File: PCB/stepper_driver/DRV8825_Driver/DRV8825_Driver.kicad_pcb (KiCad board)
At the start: 2 copper layers, 39.6 x 35.8 mm, 21 parts, among them J1 Conn_01x04_Pin, J2 Conn_01x02_Pin, J3 Conn_01x02_Pin, SW1 SW_DIP_x03, U1 DRV8825PWP

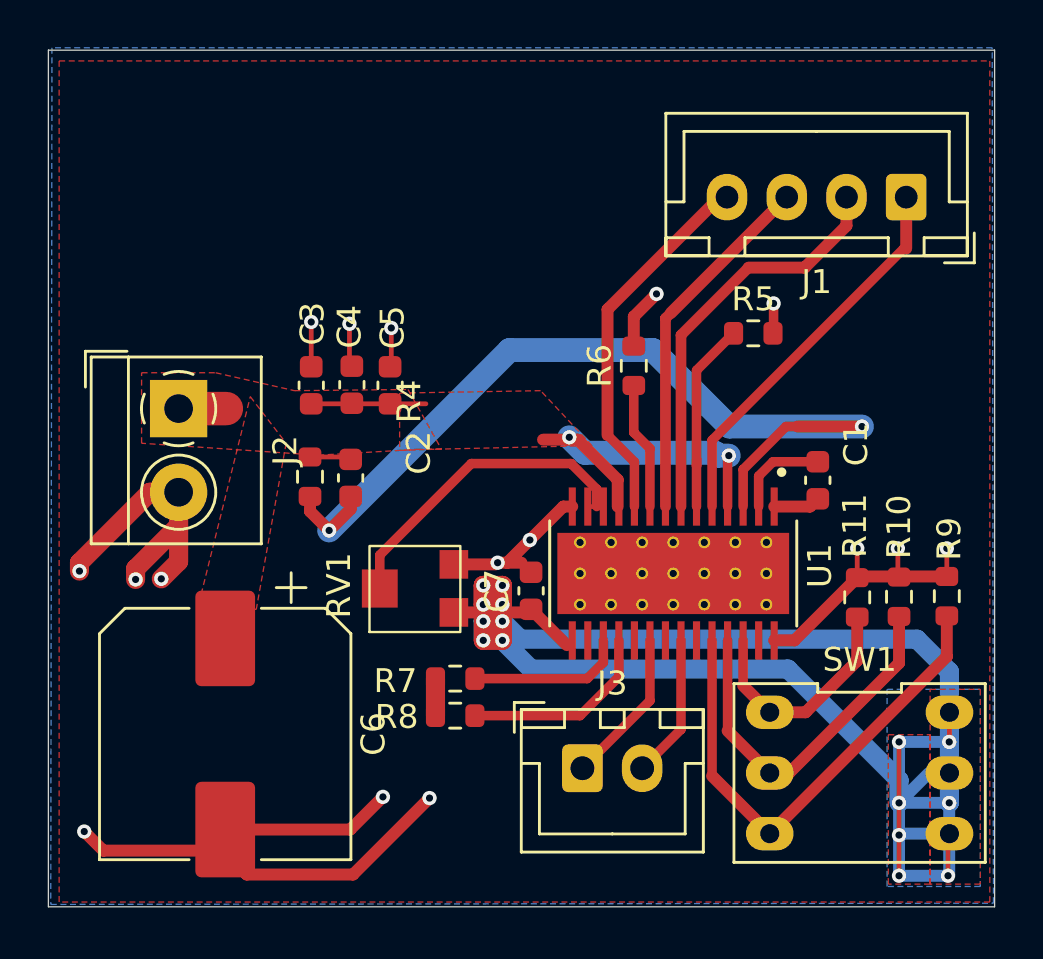
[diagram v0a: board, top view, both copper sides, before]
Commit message: footprint reduction
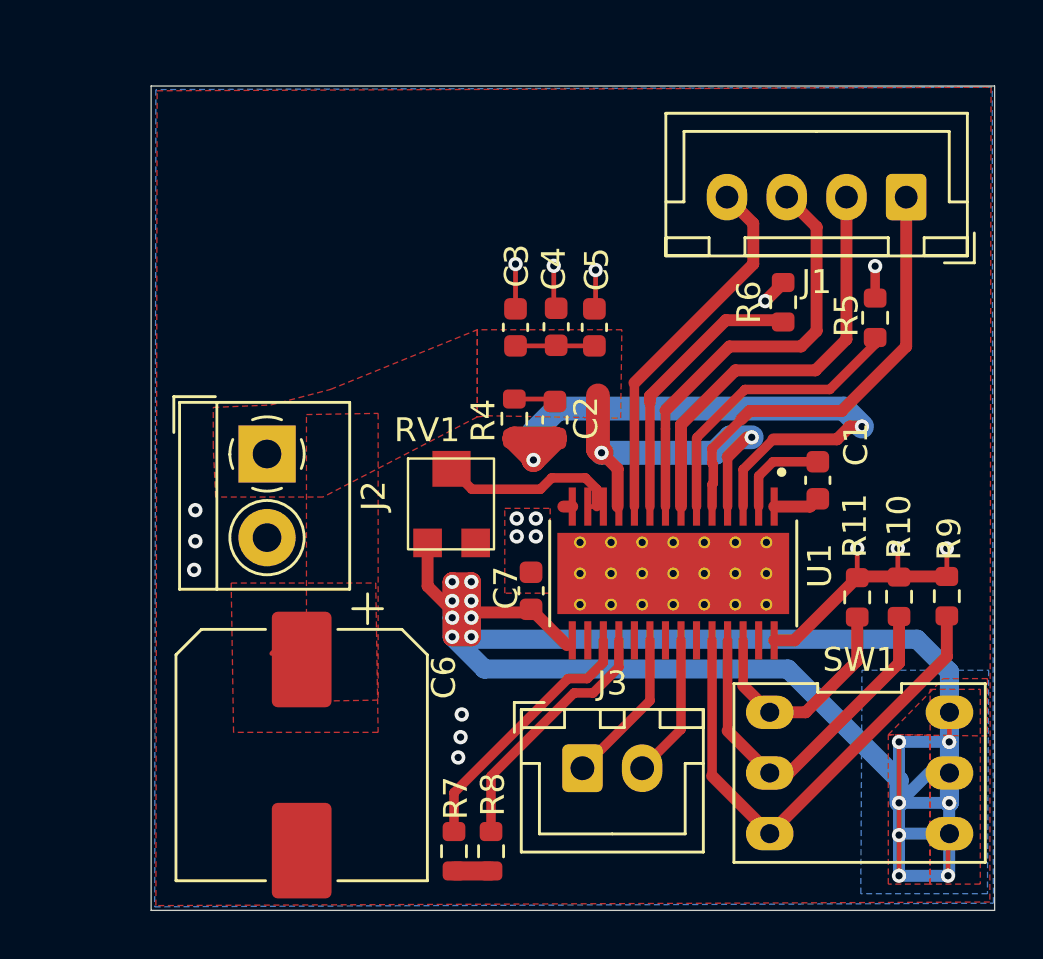
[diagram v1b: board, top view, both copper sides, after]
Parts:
- moved C3 8.89 mm to (39.9, 76.6)
- moved C2 8.89 mm to (41.5, 80.5)
- moved C5 8.89 mm to (43.1, 76.6)
- moved C4 8.89 mm to (41.5, 76.6)
- moved R4 8.89 mm to (39.8, 80.4)
- moved R7 7.23 mm to (37.3, 98.5), turned to -90 degrees
- moved R6 6.79 mm to (51.0, 75.5)
- moved R8 5.87 mm to (38.8, 98.5), turned to 90 degrees
- moved R5 5.14 mm to (54.9, 76.2), turned to 90 degrees
- moved J2 4.16 mm to (29.4, 81.9)
- moved C6 3.32 mm to (30.9, 94.5)
- moved RV1 3.15 mm to (37.2, 84.5), turned to 0 degrees
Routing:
- net gnd!: track 68.3 -> 20.1 mm, vias 16 -> 18
- net VCP: track 37.6 -> 27.2 mm
- net 3V3: track 94.1 -> 100.6 mm
- net ISENB: track 5.35 -> 11.5 mm
- net AVREF: track 13.9 -> 8.20 mm
- net NSLEEP: track 6.58 -> 11.1 mm
- net ISENA: track 8.19 -> 12.2 mm
- net BOUT2: track 15.1 -> 17.9 mm
- net NFAULT: track 8.22 -> 10.7 mm
- net AOUT1: track 16.4 -> 18.6 mm
- net VMA: track 23.9 -> 21.9 mm
- net AOUT2: track 17.2 -> 18.4 mm
- net CP2: track 4.90 -> 4.00 mm
- net BOUT1: track 15.7 -> 16.3 mm
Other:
- board size 39.6 x 35.8 mm -> 35.3 x 34.5 mm
